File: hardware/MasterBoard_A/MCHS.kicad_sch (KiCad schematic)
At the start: 24 parts, among them Q401 MMBT5550L, U401 MCP1501-40xSN, U402 TLV713185PDBV, U403 NSI5030, U404 MCP33151, U405 MCP33151, U406 MIC7300M5, U407 Si1450DH, U408 Si1450DH, U409 NCV68061

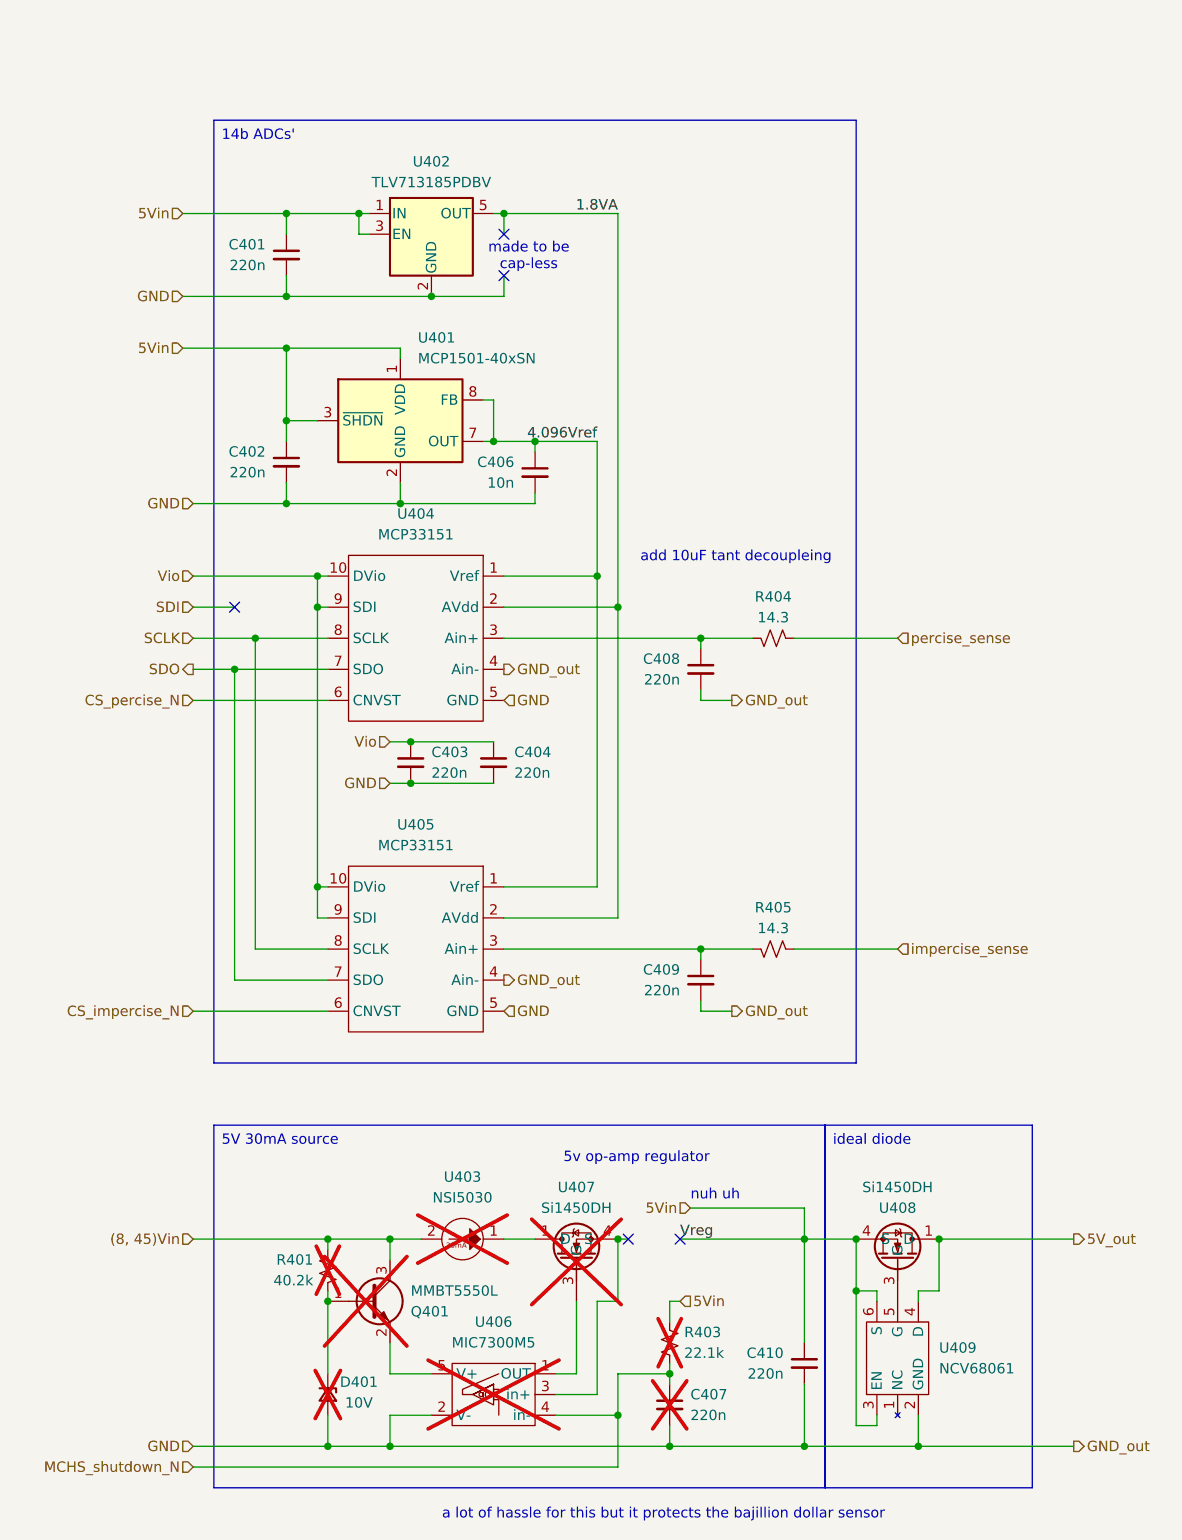
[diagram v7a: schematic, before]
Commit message: masterbaord schematic nad layout updated for v2
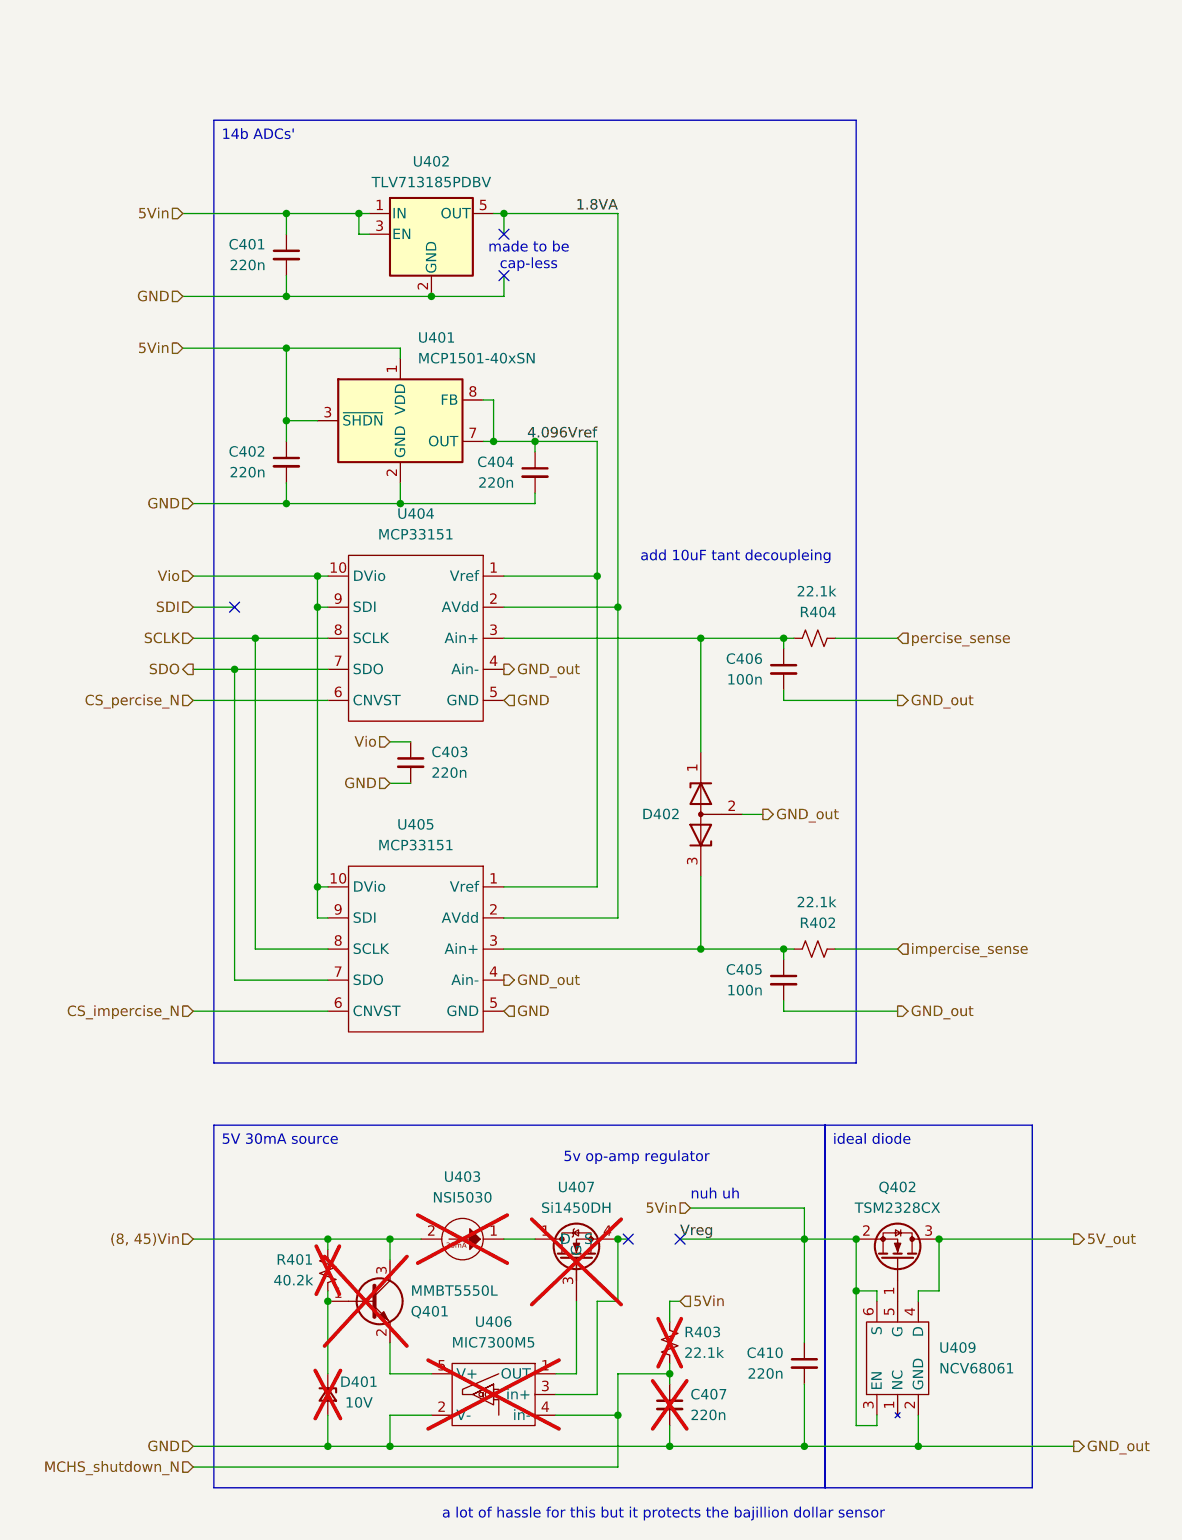
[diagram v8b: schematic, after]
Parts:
- removed C408, C409: 220n, Capacitor_SMD:C_0805_2012Metric_Pad1.18x1.45mm_HandSolder, symbol Device:C_Small
- removed R405: 14.3, Resistor_SMD:R_0805_2012Metric_Pad1.20x1.40mm_HandSolder, symbol Device:R_Small_US
- removed U408: Si1450DH, Package_TO_SOT_SMD:SOT-363_SC-70-6_Handsoldering, symbol zzLocalLibrary:Si1480DH
- added C405: 100n, Capacitor_SMD:C_0603_1608Metric_Pad1.08x0.95mm_HandSolder, symbol Device:C_Small
- added D402: D_Zener_Dual_CommonAnode_KAK, Package_TO_SOT_SMD:SOT-23, symbol Device:D_Zener_Dual_CommonAnode_KAK
- added Q402: TSM2328CX, Package_TO_SOT_SMD:SOT-23-3, symbol Transistor_FET:Q_NMOS_GSD
- added R402: 22.1k, Resistor_SMD:R_0805_2012Metric_Pad1.20x1.40mm_HandSolder, symbol Device:R_Small_US
- C401, C402, C403, C404: unit x1 (none) -> 0.14
- C406: value 10n -> 100n; footprint Capacitor_SMD:C_0805_2012Metric_Pad1.18x1.45mm_HandSolder -> Capacitor_SMD:C_0603_1608Metric_Pad1.08x0.95mm_HandSolder; mouser https://www.mouser.com/ProductDetail/KYOCERA-AVX/08051C103J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 -> https://www.mouser.com/ProductDetail/Wurth-Elektronik/88501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; specs 10nF, 5%, 100VDC, X7R, MLCC -> 100nF, 10%, 50V, X7R, -55C, +125C; unit x10 0.04 -> 0.029; unit x100 (none) -> 0.017; unit x50 (none) -> 0.02
- C410: unit x1 0.054 -> 0.14
- R404: value 14.3 -> 22.1k; mouser https://www.mouser.com/ProductDetail/KOA-Speer/RK73H2ATTD14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 -> https://www.mouser.com/ProductDetail/YAGEO/AC0805FR-0722K1L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; specs 14.3R, 250mW, 1%, 100ppm, 150V, -55C, +155C -> 22.1kR, 1%, 125mW, 150V, 100ppm, -55C, +155C; unit x10 0.02 -> 0.011
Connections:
- net 4.096Vref: now also C404.1; no longer C406.1
- net 5V_out: now also Q402.3 (D)
- net 5Vin: now also Q402.2 (S)
- net GND: now also C405.2, D402.2 (A)
- net Vio: no longer C404.1
- net impercise_sense: now also R402.1
- net at U405.3 (Ain+): now also C405.1, D402.3 (K), R402.2
- net at U409.5 (G): now also Q402.1 (G)
- net at R404.2, U404.3 (Ain+): now also C406.1, D402.1 (K)
